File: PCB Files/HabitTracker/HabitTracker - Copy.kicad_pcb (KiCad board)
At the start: 2 copper layers, 39 parts, among them U1 TLC5955DCA, U2 TLC5955DCA, U3 TLC5955DCA

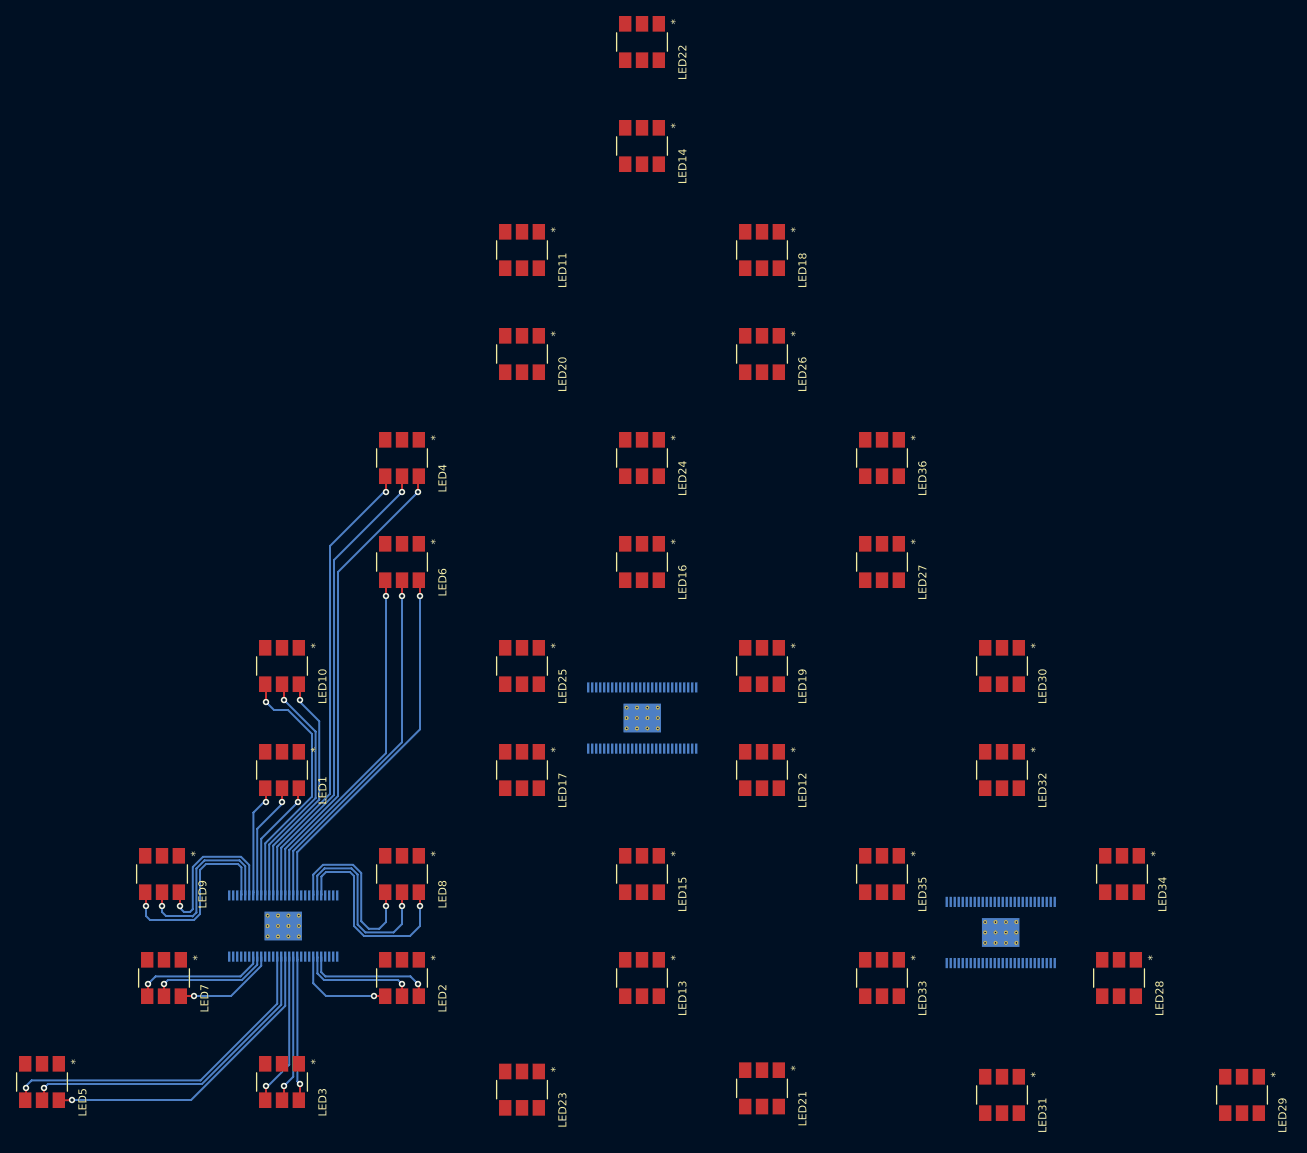
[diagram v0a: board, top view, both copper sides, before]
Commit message: Created PCB and net file
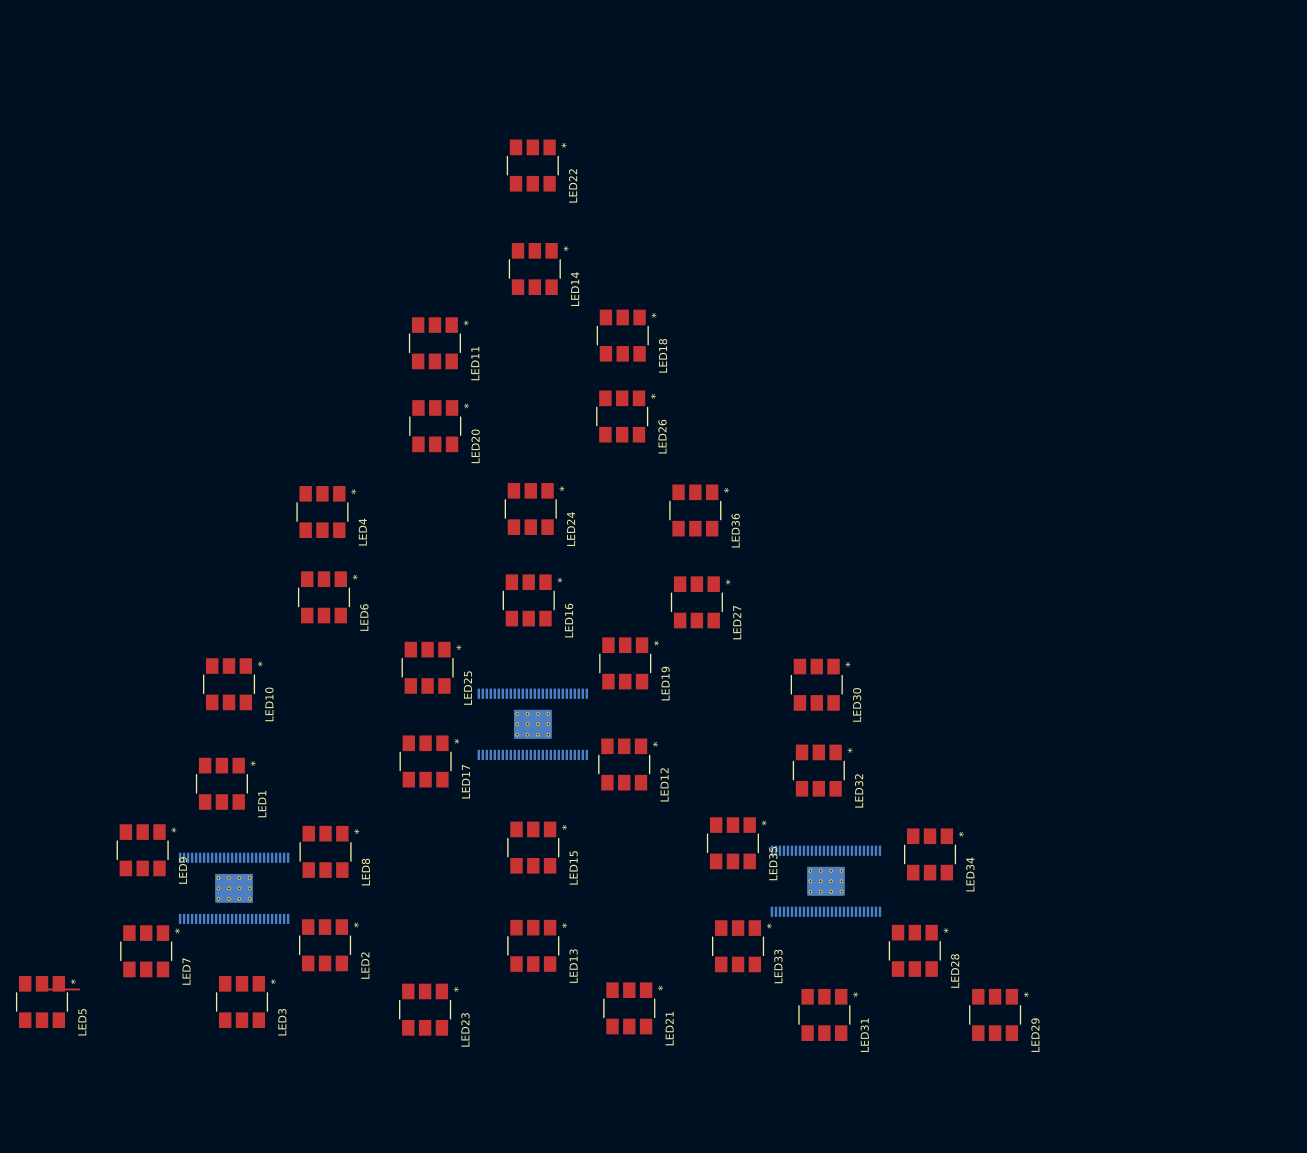
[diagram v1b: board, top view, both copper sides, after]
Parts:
- moved LED29 32.4 mm to (199.1, 141.6)
- moved LED28 25.8 mm to (189.1, 133.6)
- moved LED31 24.3 mm to (177.8, 141.6)
- moved LED36 24.2 mm to (161.7, 78.6)
- moved LED34 24.1 mm to (191.0, 121.6)
- moved LED27 23.7 mm to (161.9, 90.0)
- moved LED30 23.3 mm to (176.8, 100.3)
- moved LED32 22.9 mm to (177.1, 111.1)
- moved U3 22.8 mm to (178.0, 124.9)
- moved LED22 20.6 mm to (141.4, 35.4)
- moved LED18 20.4 mm to (152.6, 56.7)
- moved LED14 20.4 mm to (141.6, 48.4)
- moved LED21 19.4 mm to (153.4, 140.8)
- moved LED26 19.1 mm to (152.5, 66.8)
- moved LED35 19.0 mm to (166.4, 120.2)
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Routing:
- net Net-(LED4-Pad6): track 59.3 -> 0.00 mm, vias 1 -> 0
- net Net-(LED4-Pad5): track 58.7 -> 0.00 mm, vias 1 -> 0
- net Net-(LED4-Pad4): track 58.2 -> 0.00 mm, vias 1 -> 0
- net Net-(LED6-Pad6): track 45.8 -> 0.00 mm, vias 1 -> 0
- net Net-(LED6-Pad5): track 45.0 -> 0.00 mm, vias 1 -> 0
- net Net-(LED6-Pad4): track 44.5 -> 0.00 mm, vias 1 -> 0
- net Net-(LED5-Pad4): track 43.4 -> 0.00 mm, vias 1 -> 0
- net Net-(LED5-Pad5): track 41.6 -> 0.00 mm, vias 1 -> 0
- net Net-(LED5-Pad6): track 39.3 -> 0.00 mm, vias 1 -> 0
- net Net-(LED10-Pad4): track 32.3 -> 0.00 mm, vias 1 -> 0
- net Net-(LED10-Pad5): track 30.5 -> 0.00 mm, vias 1 -> 0
- net Net-(LED10-Pad6): track 29.8 -> 0.00 mm, vias 1 -> 0
- net Net-(LED8-Pad6): track 26.7 -> 0.00 mm, vias 1 -> 0
- net Net-(LED9-Pad4): track 25.0 -> 0.00 mm, vias 1 -> 0
- net Net-(LED8-Pad5): track 24.8 -> 0.00 mm, vias 1 -> 0
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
